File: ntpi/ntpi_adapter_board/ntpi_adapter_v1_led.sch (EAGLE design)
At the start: 7 parts, among them Q1 BC849C

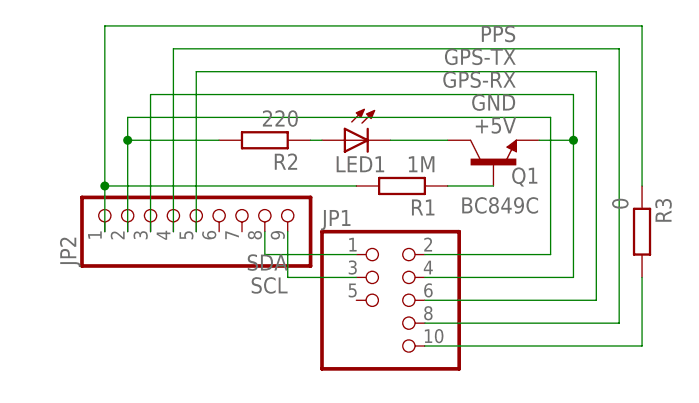
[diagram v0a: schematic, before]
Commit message: silk screen font changes
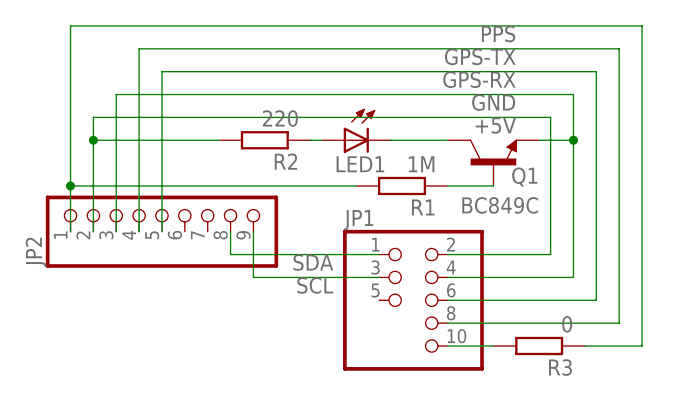
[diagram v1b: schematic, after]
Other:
- moved on the sheet: JP1, JP2, R3
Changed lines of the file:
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@@
 </plain>
 <instances>
-<instance part="JP1" gate="G$1" x="73.66" y="55.88"/>
-<instance part="JP2" gate="A" x="53.34" y="66.04" rot="R90"/>
+<instance part="JP1" gate="G$1" x="76.2" y="55.88"/>
+<instance part="JP2" gate="A" x="49.53" y="66.04" rot="R90"/>
 <instance part="R1" gate="G$1" x="76.2" y="68.58" rot="R180"/>
 <instance part="R2" gate="G$1" x="60.96" y="73.66" rot="R180"/>
@@
 </instance>
 <instance part="LED1" gate="G$1" x="69.85" y="73.66" rot="MR270"/>
-<instance part="R3" gate="G$1" x="102.87" y="63.5" rot="R270"/>
+<instance part="R3" gate="G$1" x="91.44" y="50.8" rot="R180"/>
 </instances>
 <busses>
@@
 <segment>
 <pinref part="JP1" gate="G$1" pin="2"/>
-<wire x1="78.74" y1="60.96" x2="92.71" y2="60.96" width="0.1524" layer="91"/>
+<wire x1="81.28" y1="60.96" x2="92.71" y2="60.96" width="0.1524" layer="91"/>
 <wire x1="92.71" y1="60.96" x2="92.71" y2="76.2" width="0.1524" layer="91"/>
 <pinref part="JP2" gate="A" pin="2"/>
-<wire x1="92.71" y1="76.2" x2="45.72" y2="76.2" width="0.1524" layer="91"/>
-<wire x1="45.72" y1="76.2" x2="45.72" y2="73.66" width="0.1524" layer="91"/>
+<wire x1="92.71" y1="76.2" x2="41.91" y2="76.2" width="0.1524" layer="91"/>
+<wire x1="41.91" y1="76.2" x2="41.91" y2="73.66" width="0.1524" layer="91"/>
 <label x="88.9" y="76.2" size="1.778" layer="95" rot="R180"/>
 <pinref part="R2" gate="G$1" pin="2"/>
-<wire x1="45.72" y1="73.66" x2="45.72" y2="63.5" width="0.1524" layer="91"/>
-<wire x1="55.88" y1="73.66" x2="45.72" y2="73.66" width="0.1524" layer="91"/>
-<junction x="45.72" y="73.66"/>
+<wire x1="41.91" y1="73.66" x2="41.91" y2="63.5" width="0.1524" layer="91"/>
+<wire x1="55.88" y1="73.66" x2="41.91" y2="73.66" width="0.1524" layer="91"/>
+<junction x="41.91" y="73.66"/>
 </segment>
 </net>
@@
 <segment>
 <pinref part="JP1" gate="G$1" pin="4"/>
-<wire x1="78.74" y1="58.42" x2="95.25" y2="58.42" width="0.1524" layer="91"/>
+<wire x1="81.28" y1="58.42" x2="95.25" y2="58.42" width="0.1524" layer="91"/>
 <wire x1="95.25" y1="58.42" x2="95.25" y2="73.66" width="0.1524" layer="91"/>
 <pinref part="JP2" gate="A" pin="3"/>
 <wire x1="95.25" y1="73.66" x2="95.25" y2="78.74" width="0.1524" layer="91"/>
-<wire x1="95.25" y1="78.74" x2="48.26" y2="78.74" width="0.1524" layer="91"/>
-<wire x1="48.26" y1="78.74" x2="48.26" y2="63.5" width="0.1524" layer="91"/>
+<wire x1="95.25" y1="78.74" x2="44.45" y2="78.74" width="0.1524" layer="91"/>
+<wire x1="44.45" y1="78.74" x2="44.45" y2="63.5" width="0.1524" layer="91"/>
 <label x="88.9" y="78.74" size="1.778" layer="95" rot="R180"/>
 <pinref part="Q1" gate="G$1" pin="E"/>
@@
 <segment>
 <pinref part="JP1" gate="G$1" pin="6"/>
-<wire x1="78.74" y1="55.88" x2="97.79" y2="55.88" width="0.1524" layer="91"/>
+<wire x1="81.28" y1="55.88" x2="97.79" y2="55.88" width="0.1524" layer="91"/>
 <wire x1="97.79" y1="55.88" x2="97.79" y2="81.28" width="0.1524" layer="91"/>
-<wire x1="97.79" y1="81.28" x2="53.34" y2="81.28" width="0.1524" layer="91"/>
+<wire x1="97.79" y1="81.28" x2="49.53" y2="81.28" width="0.1524" layer="91"/>
 <pinref part="JP2" gate="A" pin="5"/>
-<wire x1="53.34" y1="63.5" x2="53.34" y2="81.28" width="0.1524" layer="91"/>
+<wire x1="49.53" y1="63.5" x2="49.53" y2="81.28" width="0.1524" layer="91"/>
 <label x="88.9" y="81.28" size="1.778" layer="95" rot="R180"/>
 </segment>
@@
 <segment>
 <pinref part="JP1" gate="G$1" pin="8"/>
-<wire x1="78.74" y1="53.34" x2="100.33" y2="53.34" width="0.1524" layer="91"/>
+<wire x1="81.28" y1="53.34" x2="100.33" y2="53.34" width="0.1524" layer="91"/>
 <wire x1="100.33" y1="53.34" x2="100.33" y2="83.82" width="0.1524" layer="91"/>
-<wire x1="100.33" y1="83.82" x2="50.8" y2="83.82" width="0.1524" layer="91"/>
+<wire x1="100.33" y1="83.82" x2="46.99" y2="83.82" width="0.1524" layer="91"/>
 <pinref part="JP2" gate="A" pin="4"/>
-<wire x1="50.8" y1="63.5" x2="50.8" y2="83.82" width="0.1524" layer="91"/>
+<wire x1="46.99" y1="63.5" x2="46.99" y2="83.82" width="0.1524" layer="91"/>
 <label x="88.9" y="83.82" size="1.778" layer="95" rot="R180"/>
 </segment>
@@
 <segment>
 <pinref part="JP1" gate="G$1" pin="1"/>
-<wire x1="71.12" y1="60.96" x2="60.96" y2="60.96" width="0.1524" layer="91"/>
+<wire x1="73.66" y1="60.96" x2="57.15" y2="60.96" width="0.1524" layer="91"/>
 <pinref part="JP2" gate="A" pin="8"/>
-<wire x1="60.96" y1="60.96" x2="60.96" y2="63.5" width="0.1524" layer="91"/>
-<label x="63.5" y="60.96" size="1.778" layer="95" rot="R180"/>
+<wire x1="57.15" y1="60.96" x2="57.15" y2="63.5" width="0.1524" layer="91"/>
+<label x="68.58" y="60.96" size="1.778" layer="95" rot="R180"/>
 </segment>
 </net>
@@
 <segment>
 <pinref part="JP1" gate="G$1" pin="3"/>
-<wire x1="71.12" y1="58.42" x2="63.5" y2="58.42" width="0.1524" layer="91"/>
+<wire x1="73.66" y1="58.42" x2="59.69" y2="58.42" width="0.1524" layer="91"/>
 <pinref part="JP2" gate="A" pin="9"/>
-<wire x1="63.5" y1="58.42" x2="63.5" y2="63.5" width="0.1524" layer="91"/>
-<label x="63.5" y="58.42" size="1.778" layer="95" rot="R180"/>
+<wire x1="59.69" y1="58.42" x2="59.69" y2="63.5" width="0.1524" layer="91"/>
+<label x="68.58" y="58.42" size="1.778" layer="95" rot="R180"/>
 </segment>
 </net>
 <net name="PPS" class="0">
 <segment>
-<wire x1="102.87" y1="86.36" x2="43.18" y2="86.36" width="0.1524" layer="91"/>
+<wire x1="102.87" y1="86.36" x2="39.37" y2="86.36" width="0.1524" layer="91"/>
 <pinref part="JP2" gate="A" pin="1"/>
-<wire x1="43.18" y1="86.36" x2="43.18" y2="68.58" width="0.1524" layer="91"/>
+<wire x1="39.37" y1="86.36" x2="39.37" y2="68.58" width="0.1524" layer="91"/>
 <label x="88.9" y="86.36" size="1.778" layer="95" rot="R180"/>
 <pinref part="R3" gate="G$1" pin="1"/>
-<wire x1="43.18" y1="68.58" x2="43.18" y2="63.5" width="0.1524" layer="91"/>
-<wire x1="102.87" y1="68.58" x2="102.87" y2="86.36" width="0.1524" layer="91"/>
+<wire x1="39.37" y1="68.58" x2="39.37" y2="63.5" width="0.1524" layer="91"/>
+<wire x1="96.52" y1="50.8" x2="102.87" y2="50.8" width="0.1524" layer="91"/>
+<wire x1="102.87" y1="50.8" x2="102.87" y2="86.36" width="0.1524" layer="91"/>
 <pinref part="R1" gate="G$1" pin="2"/>
-<wire x1="71.12" y1="68.58" x2="43.18" y2="68.58" width="0.1524" layer="91"/>
-<junction x="43.18" y="68.58"/>
+<wire x1="71.12" y1="68.58" x2="39.37" y2="68.58" width="0.1524" layer="91"/>
+<junction x="39.37" y="68.58"/>
 </segment>
 </net>
@@
 <segment>
 <pinref part="JP1" gate="G$1" pin="10"/>
-<wire x1="78.74" y1="50.8" x2="102.87" y2="50.8" width="0.1524" layer="91"/>
+<wire x1="81.28" y1="50.8" x2="86.36" y2="50.8" width="0.1524" layer="91"/>
 <pinref part="R3" gate="G$1" pin="2"/>
-<wire x1="102.87" y1="58.42" x2="102.87" y2="50.8" width="0.1524" layer="91"/>
 </segment>
 </net>
